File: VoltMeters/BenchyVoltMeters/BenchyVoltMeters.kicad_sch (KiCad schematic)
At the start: 2 parts, among them J2 DSUB-26, J3 MB-COMMS

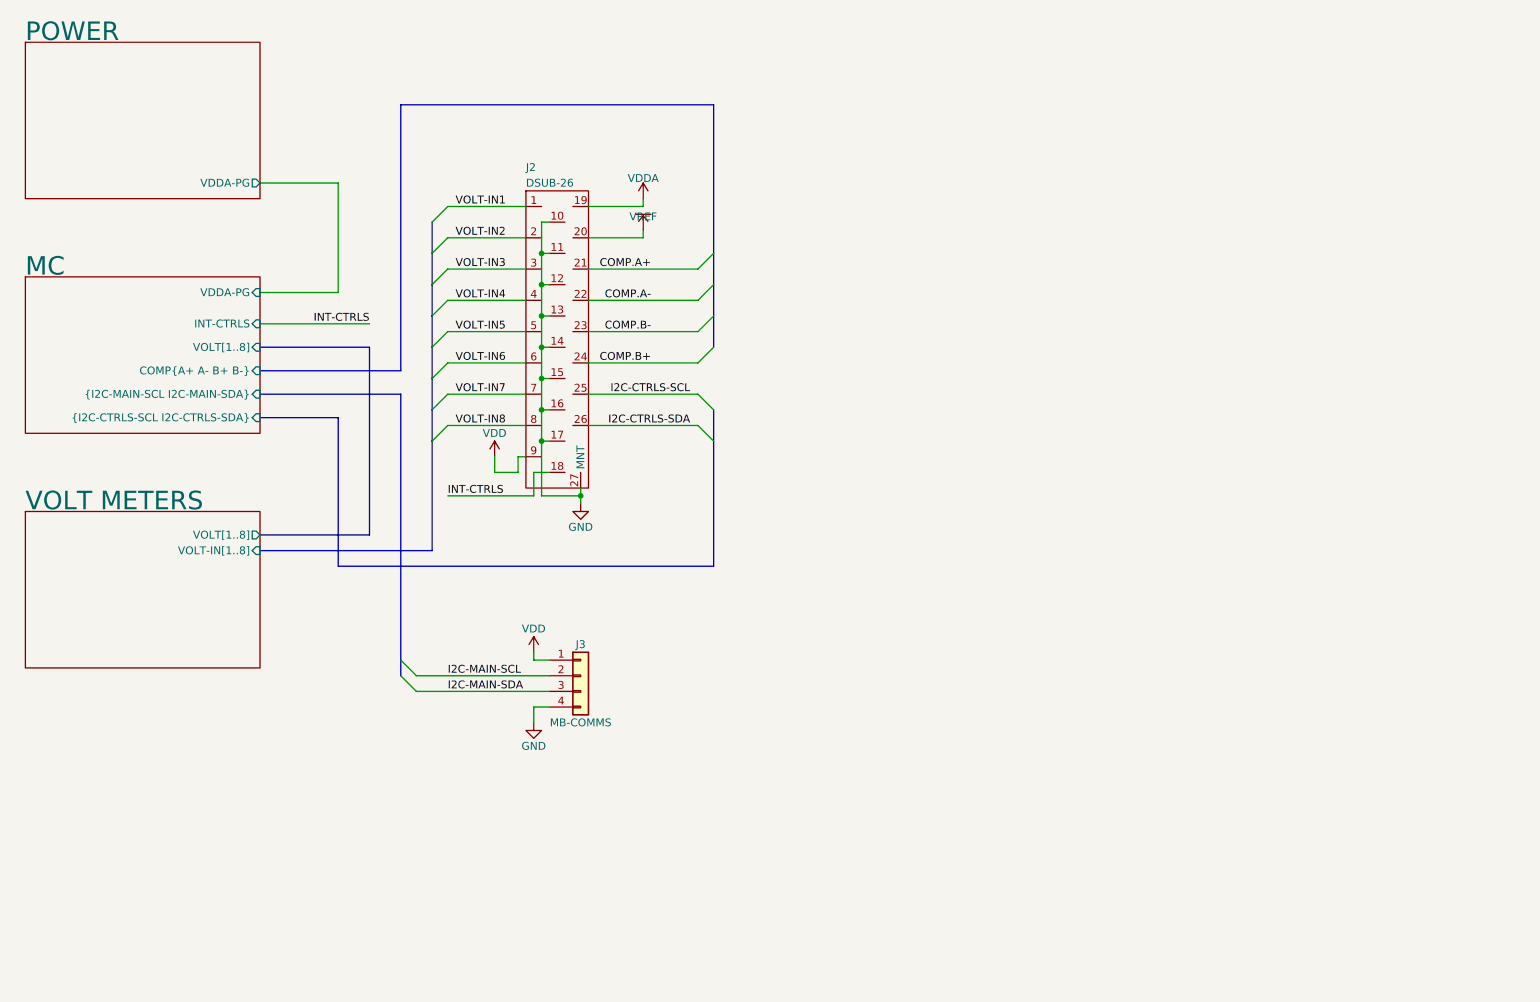
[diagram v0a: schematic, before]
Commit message: Add voltmeter PCB
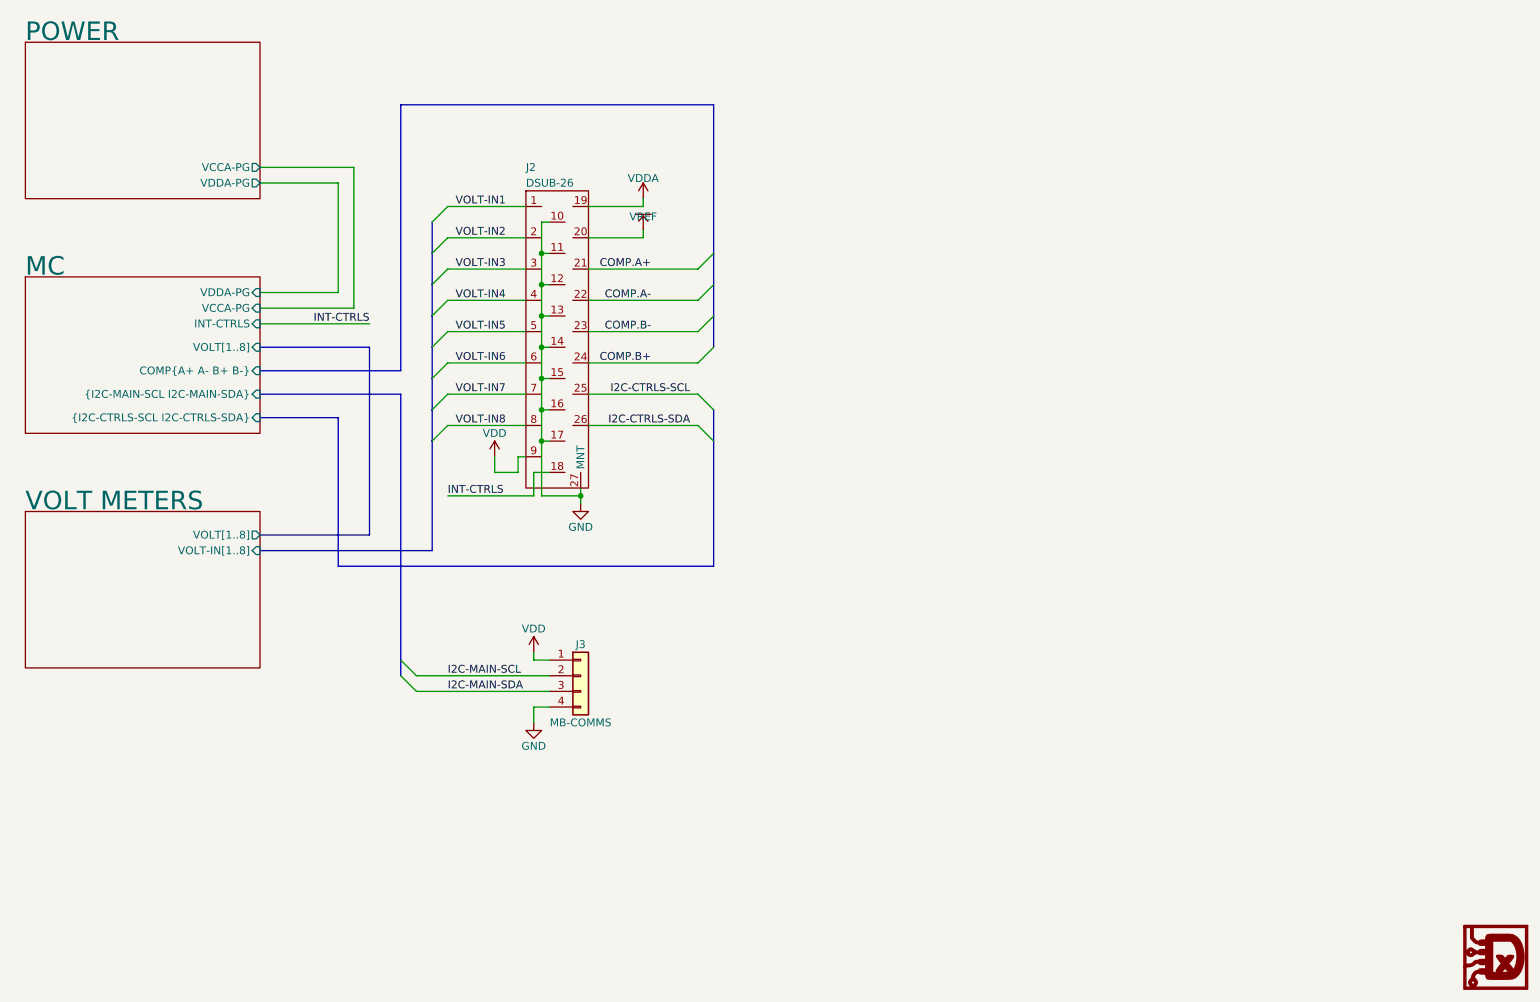
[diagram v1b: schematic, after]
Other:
- sheet MC ports: added VCCA-PG; removed none
- sheet POWER ports: added VCCA-PG; removed none
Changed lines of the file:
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@@
+    (stroke (width 0) (type default))
+  )
+  (wire (pts (xy 91.44 45.72) (xy 76.2 45.72))
     (stroke (width 0) (type default))
   )
@@
     (stroke (width 0) (type default))
   )
+  (wire (pts (xy 76.2 68.58) (xy 91.44 68.58))
+    (stroke (width 0) (type default))
+  )
   (bus (pts (xy 76.2 78.74) (xy 99.06 78.74))
     (stroke (width 0) (type default))
@@
   )
   (wire (pts (xy 101.6 128.27) (xy 123.19 128.27))
+    (stroke (width 0) (type default))
+  )
+  (wire (pts (xy 91.44 68.58) (xy 91.44 45.72))
     (stroke (width 0) (type default))
   )
@@
         (path "/0c37bca8-710a-4b7e-9f67-d722ace534a9"
           (reference "#PWR044") (unit 1)
+        )
+      )
+    )
+  )
+  (symbol (lib_id "Daxxn_Logos:LOGO") (at 276.86 173.99 0) (unit 1)
+    (in_bom no) (on_board yes) (dnp no)
+    (property "Reference" "#G1" (at 276.86 167.894 0)
+      (effects (font (size 1.27 1.27)) hide)
+    )
+    (property "Value" "LOGO" (at 276.86 166.37 0)
+      (effects (font (size 1.27 1.27)) hide)
+    )
+    (property "Footprint" "" (at 276.86 164.465 0)
+      (effects (font (size 1.27 1.27)) hide)
+    )
+    (property "Datasheet" "" (at 276.86 173.99 0)
+      (effects (font (size 1.27 1.27)) hide)
+    )
+    (property "Schematic" "" (at 276.86 173.99 0)
+      (effects (font (size 1.27 1.27)) hide)
+    )
+    (property "PartNumber" "" (at 276.86 173.99 0)
+      (effects (font (size 1.27 1.27)) hide)
+    )
+    (property "SupplierPN" "" (at 276.86 173.99 0)
+      (effects (font (size 1.27 1.27)) hide)
+    )
+    (property "Sim.Enable" "0" (at 276.86 173.99 0)
+      (effects (font (size 1.27 1.27)) hide)
+    )
+    (instances
+      (project "BenchyVoltMeters"
+        (path "/0c37bca8-710a-4b7e-9f67-d722ace534a9"
+          (reference "#G1") (unit 1)
         )
       )
@@
       (effects (font (size 1.27 1.27)) (justify right))
     )
+    (pin "VCCA-PG" input (at 76.2 68.58 0)
+      (effects (font (size 1.27 1.27)) (justify right))
+    )
     (instances
       (project "BenchyVoltMeters"
@@
       (effects (font (size 1.27 1.27)) (justify right))
     )
+    (pin "VCCA-PG" output (at 76.2 45.72 0)
+      (effects (font (size 1.27 1.27)) (justify right))
+    )
